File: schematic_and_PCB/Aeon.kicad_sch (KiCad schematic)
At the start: 131 parts, among them IC1 AEM10941-QFN, IC2 STM32L412K8T6, IC3 FM25L04B-GTR, IC4 TPS7A0233PDBVR, J1 Conn_01x06_Pin, J2 FH34SRJ-50S-0.5SH50 - Colour 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, J3 Micro_SD_Card, Q1 BSS138, Q2 SI2301CDS-T1-E3, Q4 SI2301CDS-T1-E3, Q5 BSS138, SW1 SW_EHV_EN, SW2 REFRESH_BTN, SW3 RESET_BTN, SW4 SW_DIP_x06_SMD_1.27, SW5 SW_DIP_x06_SMD_1.27

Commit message: Change electrical design to match Spectra 6 driver reference
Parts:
- removed TP22, TP23, TP31: ~, TestPoint:TestPoint_Pad_D1.0mm, symbol Connector:TestPoint
- added C43, C44, C45, C6: 100nF/50V, Capacitor_SMD:C_0603_1608Metric_Pad1.08x0.95mm_HandSolder, symbol Device:C_Small
- added D7: BZT52C27, Diode_SMD:D_SOD-123, symbol Device:D_Zener
- C15, C16: value 10uF/25V -> 1uF/50V; Link https://au.mouser.com/ProductDetail/Samsung-Electro-Mechani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 -> https://www.aliexpress.com/item/1005007464553853.html; Purchase Qty See other -> 50; Store Mouser -> Aliexpress
- C17: value 2.2uF/6V -> 2.2uF/6.3V
- C18, C19, C20, C21: value 1uF/10V -> 1uF/50V; Link https://au.mouser.com/ProductDetail/Samsung-Electro-Mechani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 -> https://www.aliexpress.com/item/1005007464553853.html; Purchase Qty 100 -> 50; Store Mouser -> Aliexpress
- C23, C7: value 4.7uF/10V -> 4.7uF/25V
- IC4: footprint SOT95P280X145-5N -> Aeon:SOT95P280X145-5N
- JP1, JP2, JP3: footprint Jumper:SolderJumper-3_P1.3mm_Open_RoundedPad1.0x1.5mm -> Aeon:SolderJumper-3_P1.3mm_Bridged2Bar23_RoundedPad1.0x1.5mm; symbol Jumper:SolderJumper_3_Open -> Aeon:SolderJumper_3_Bridged23
- JP5, JP6, JP7: footprint Jumper:SolderJumper-2_P1.3mm_Open_RoundedPad1.0x1.5mm -> Jumper:SolderJumper-2_P1.3mm_Bridged_RoundedPad1.0x1.5mm; symbol Jumper:SolderJumper_2_Open -> Jumper:SolderJumper_2_Bridged
- JP8, JP9: footprint Jumper:SolderJumper-3_P1.3mm_Open_RoundedPad1.0x1.5mm -> Aeon:SolderJumper-3_P1.3mm_Bridged2Bar12_RoundedPad1.0x1.5mm; symbol Jumper:SolderJumper_3_Open -> Jumper:SolderJumper_3_Bridged12
- Q1: value BSS138 -> SI1308EDL; footprint Package_TO_SOT_SMD:SOT-23 -> Package_TO_SOT_SMD:SOT-323_SC-70; Link https://au.mouser.com/ProductDetail/Nexperia/BSS138AK-QR?qs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 -> https://au.mouser.com/ProductDetail/Vishay-Semiconductors/S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
- R4, R6: value 0.47R -> 0.2R; Link https://au.mouser.com/ProductDetail/Bourns/CRL0603-JW-R470E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 -> https://www.aliexpress.com/item/32917594228.html; Store Mouser -> Aliexpress
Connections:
- net +3.3V AUX: now also C6.2
- net DISP_VGL: now also C43.2
- net DISP_VPC: now also C45.2
- net DISP_VPH: now also C44.2
- net GND: now also C43.1, C44.1, C45.1, C6.1, D7.2 (A)
- net at C26.2, D2.2 (A), L3.2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: now also D7.1 (K)
- no-connect marks 12 -> 17
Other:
- note added: "BAL should be shorted to GND if not using two storage elements"
- note added: "Changelog v2.0 + Changes to match Spectra 6 Reference Design"
- note added: "MPP 70% default (lowest possible value, recommended since solar cells exposed to lower light compared to sun)"
- note added: "Set storage element voltage thresholds using solder bridges (Li-ion levels set by default)"
- note added: "Used instead of AEM10941 LDO due to peak power requirements"
- note added: "Waveshare 7.3inch Spectra 6 E-Paper Display https://www.waveshare.com/7.3inch-e-paper-hat-e.htm"
- note added: "Will be limited to ≤5V by D1"
- note removed: "Changelog v1.0 + Initial Design v1.1 + Fixed Q3 BJT incorrect footprint + Connected BOOT0 to GND + Added mounting holes + Reversed display ribbon cable connector pin order (to flip PCB mounting relative to display) + Added large capacitors near AUX switch to prevent voltage sag when AUX rail enabled + Added MCU reset pushbutton v1.2 + Added solder jumpers and unpopulated resistor pads on reverse 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"
- note removed: "MPP 70% recommended (lowest possible value, since EHV_SRC panels will be running at very low light compared to sun)"
- note removed: "Set storage element voltage thresholds using solder bridges"
- note removed: "Will be limited to ≤5V"
- moved on the sheet: C23, C24, C25, C26, C27, C28, D5, L3, L4, Q1, Q2, R3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

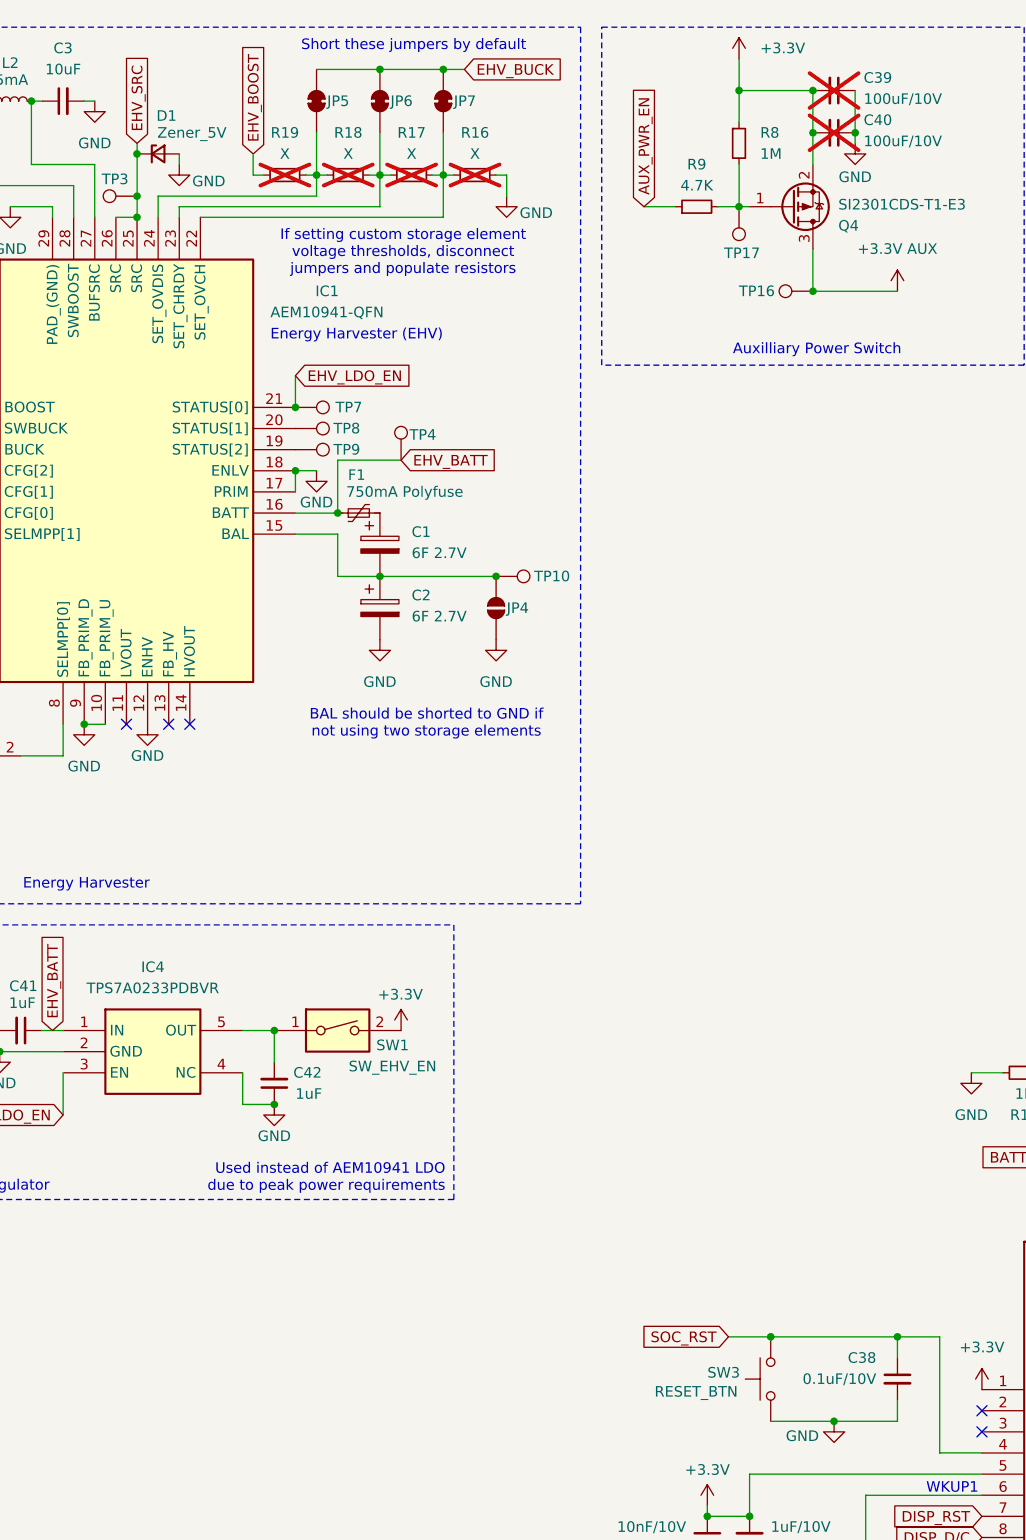
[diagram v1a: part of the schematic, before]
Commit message: Update schematic component values
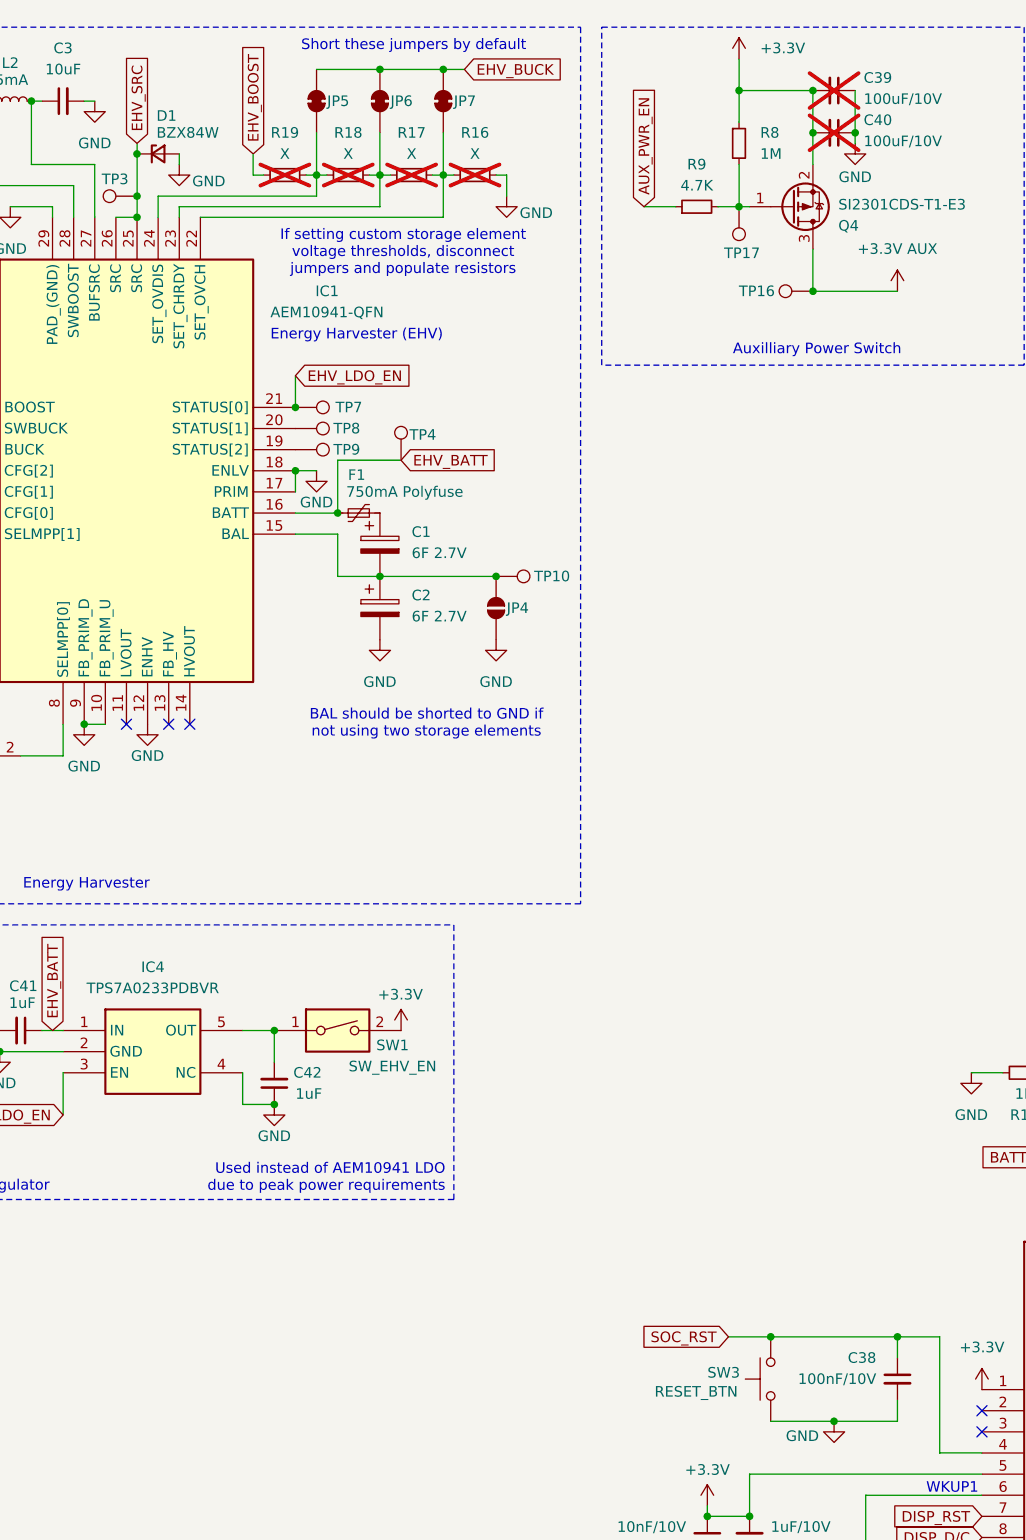
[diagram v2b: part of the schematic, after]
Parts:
- C38: value 0.1uF/10V -> 100nF/10V
- D1: value Zener_5V -> BZX84W
- TP1, TP10, TP11, TP12, TP13, TP14, TP15, TP16, TP17, TP18, TP19, TP2, TP20, TP21, TP24, TP25, TP26, TP27, TP28, TP29, TP3, TP30, TP4, TP5, TP6, TP7, TP8, TP9: value ~ -> (none)
